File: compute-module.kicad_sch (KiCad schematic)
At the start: 101 parts, among them J201 Socket_Hirose_DF40_2x50_DF40H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, J202 Socket_Hirose_DF40_2x50_DF40H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, M201 Compute-Module-4_H1.5mm, Q201 PJE138K, Q202 SSM3J332R, Q203 SSM3J332R, Q204 SSM3J332R, Q205 SSM3J332R, Q206 PJE138K, Q207 PJE138K, Q208 PJE138K, Q209 PJE138K, Q210 PJE138K, Q211 PJE138K, Q212 SSM3J332R, Q213 PJE138K, U201 TXB0104_UQFN, U203 TXB0104_UQFN, U204 MCP23017T-E_QFN

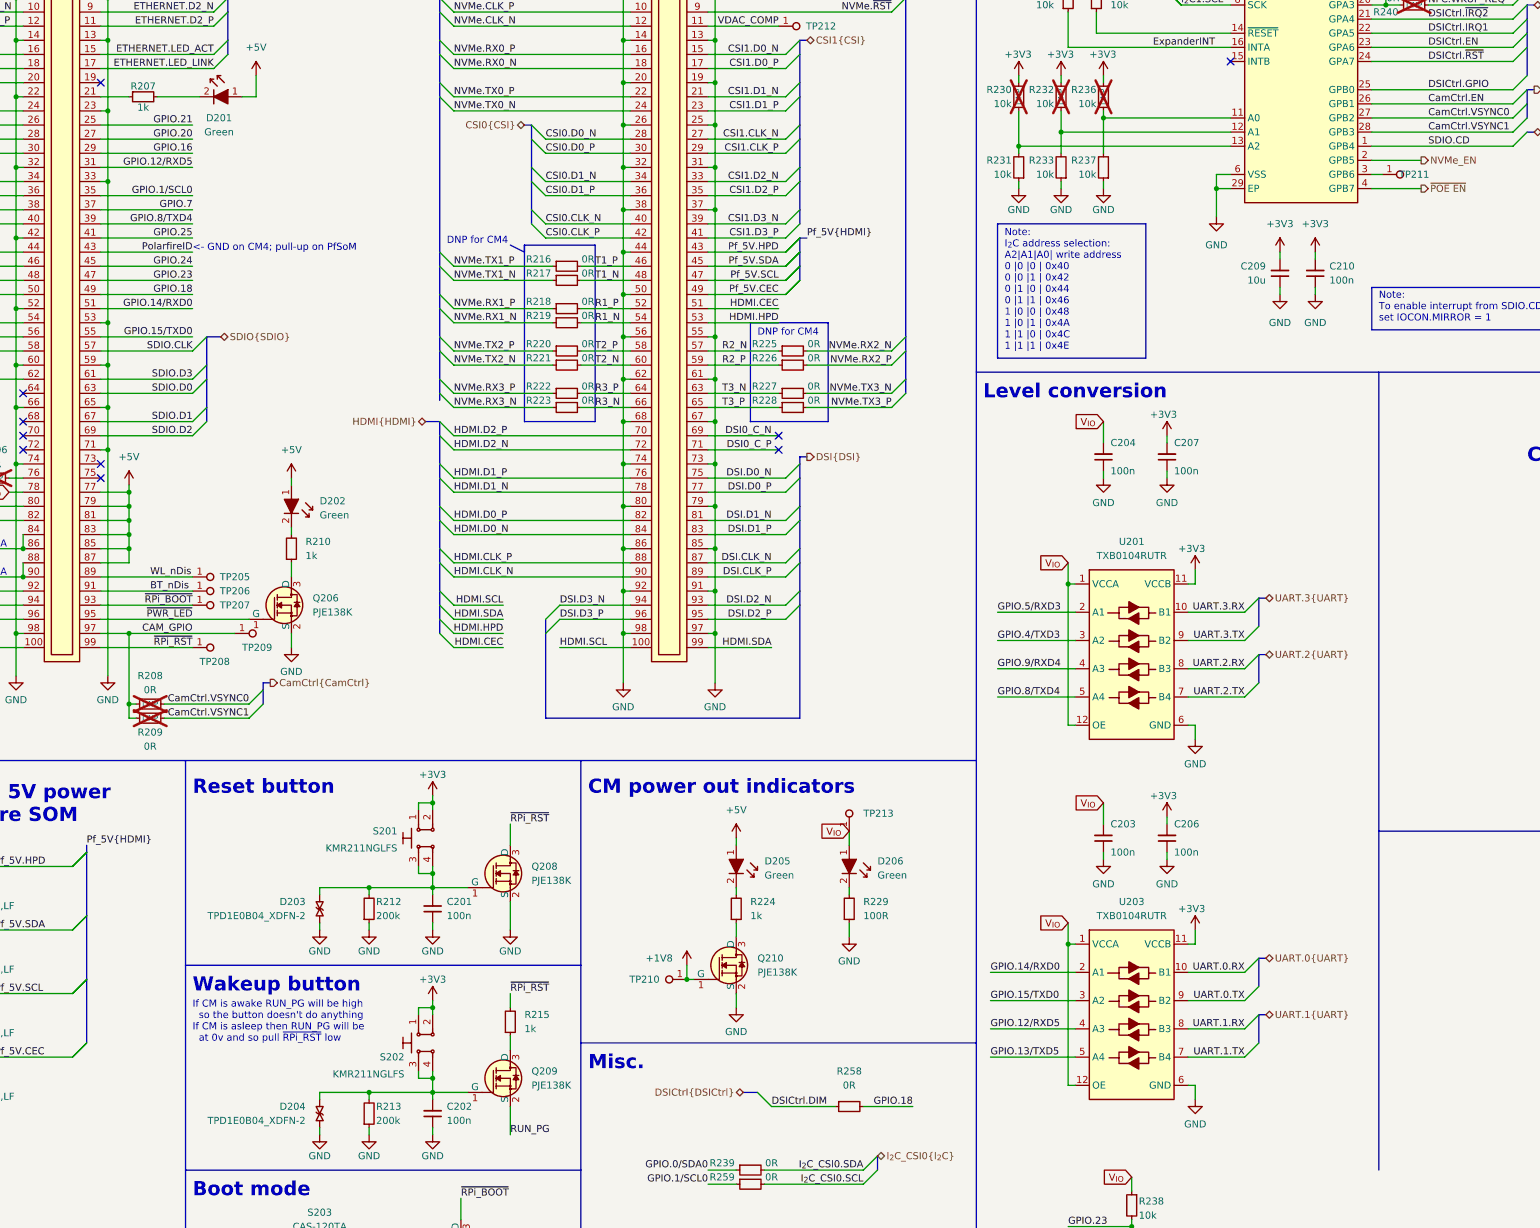
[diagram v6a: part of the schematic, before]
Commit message: [#58122] LED related fixes & improvements
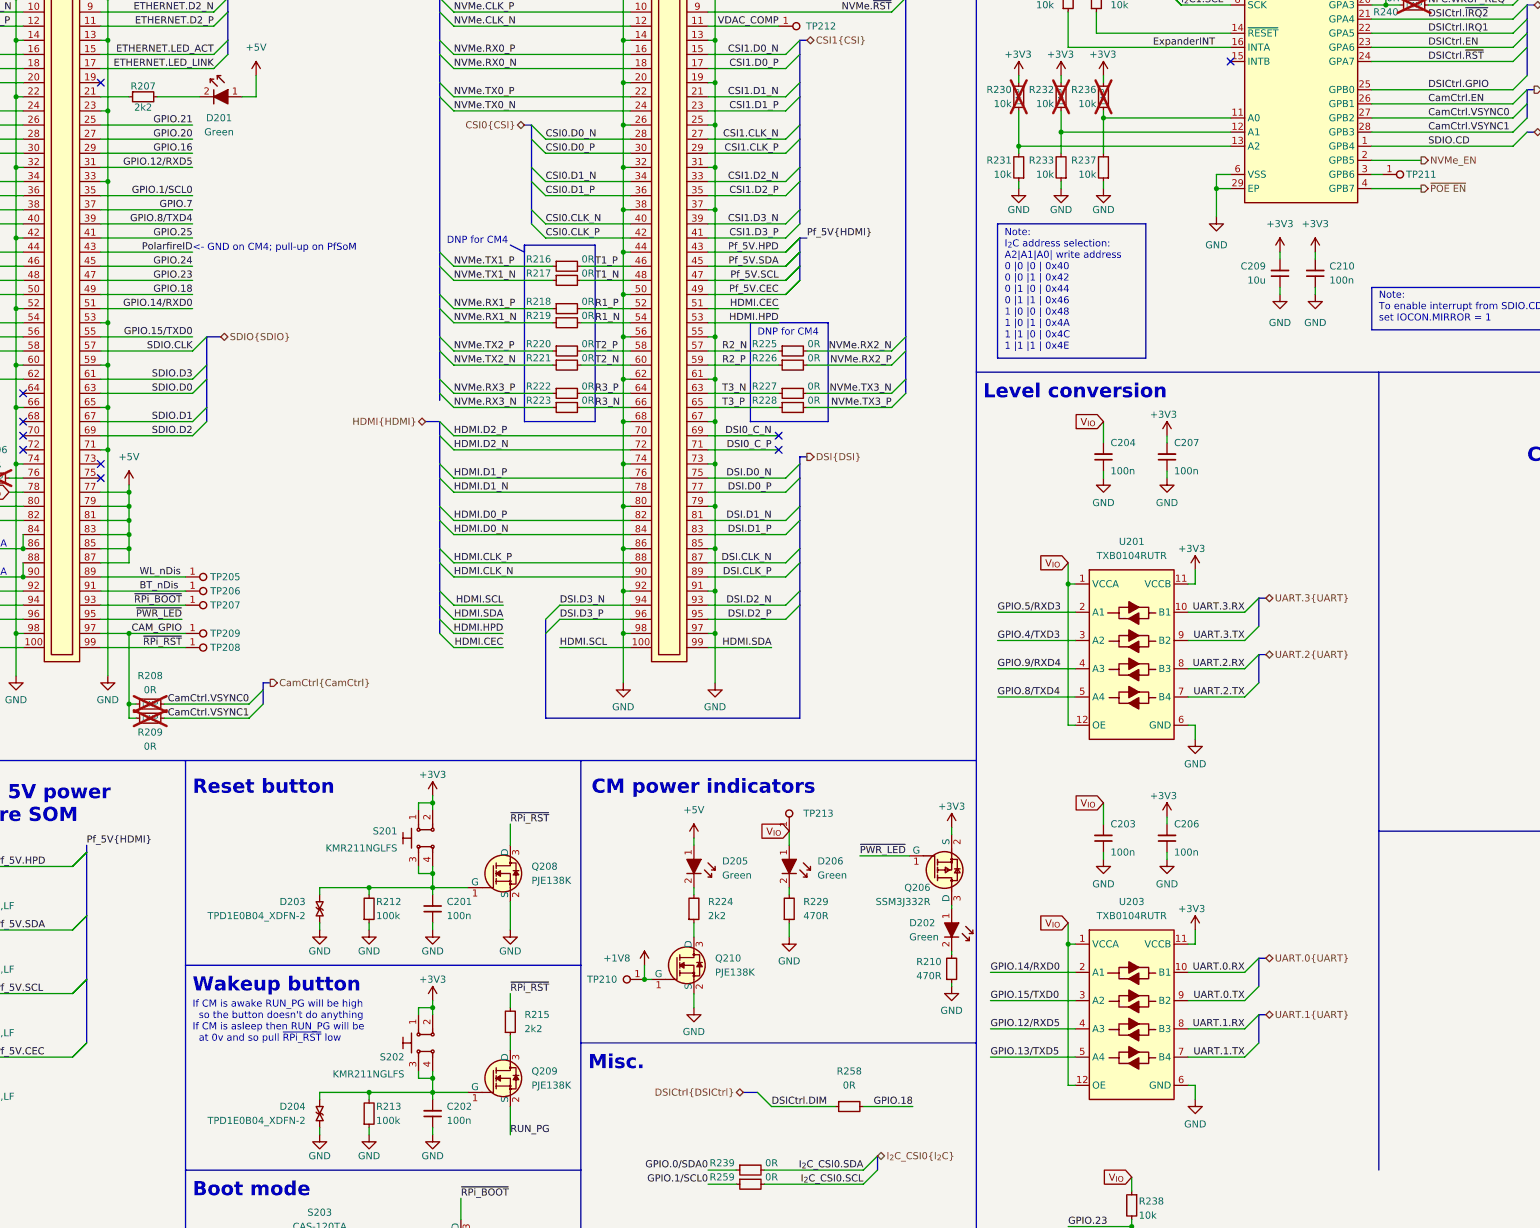
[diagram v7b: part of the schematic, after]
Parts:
- Q206: value PJE138K -> SSM3J332R; footprint antmicro-footprints:SOT-523 -> antmicro-footprints:SOT-23-3; symbol antmicroTransistorsFETsMOSFETsSingle:PJE138K -> antmicroTransistorsFETsMOSFETsSingle:SSM3J332R; MPN PJE138K_R1_00001 -> SSM3J332R,LF; Manufacturer PANJIT -> Toshiba
- R207, R215, R224: value R_1k_0402 -> R_2k2_0402; symbol antmicroResistors0402:R_1k_0402 -> antmicroResistors0402:R_2k2_0402; MPN CR0402-FX-1001GLF -> CR0402-FX-2201GLF; Val 1k -> 2k2
- R210: value R_1k_0402 -> R_470R_0402; symbol antmicroResistors0402:R_1k_0402 -> antmicroResistors0402:R_470R_0402; MPN CR0402-FX-1001GLF -> CR0402-FX-4700GLF; Val 1k -> 470R
- R212, R213: value R_200k_0402 -> R_100k_0402; symbol antmicroResistors0402:R_200k_0402 -> antmicroResistors0402:R_100k_0402; MPN CR0402-FX-2003GLF -> CR0402-FX-1003GLF; Val 200k -> 100k
- R229: value R_100R_0402 -> R_470R_0402; symbol antmicroResistors0402:R_100R_0402 -> antmicroResistors0402:R_470R_0402; MPN CR0402-FX-1000GLF -> CR0402-FX-4700GLF; Val 100R -> 470R
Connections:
- net +3V3: now also Q206.2 (S)
- net +5V: no longer D202.1
- net GND: now also R210.1; no longer Q206.2 (S)
- net at Q206.3 (D): now also D202.1; no longer R210.1
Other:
- note added: "CM power indicators"
- note removed: "CM power out indicators"
- moved on the sheet: D202, D205, D206, Q210, R210, R224, R229, TP205, TP206, TP207, TP208, TP209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
